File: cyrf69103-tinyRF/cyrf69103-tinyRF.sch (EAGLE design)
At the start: 32 parts

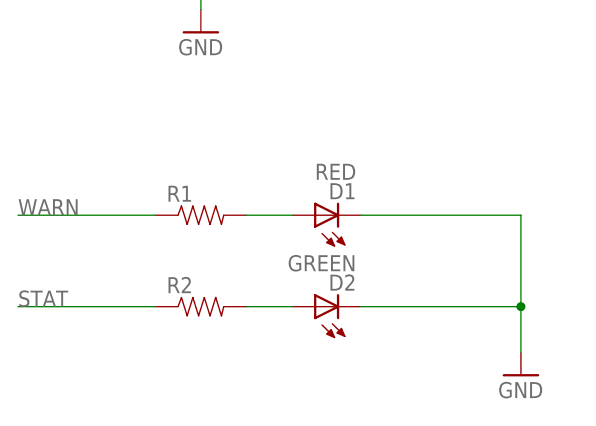
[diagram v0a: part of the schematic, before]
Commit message: Screwed up that last commit.  this update include changes to the production gerber folders.  Adds hackvana to the cyrf6936-BoB and cleans up the fab notes a bit.  Still need to standardize and parameterize the creation of the gerbers.
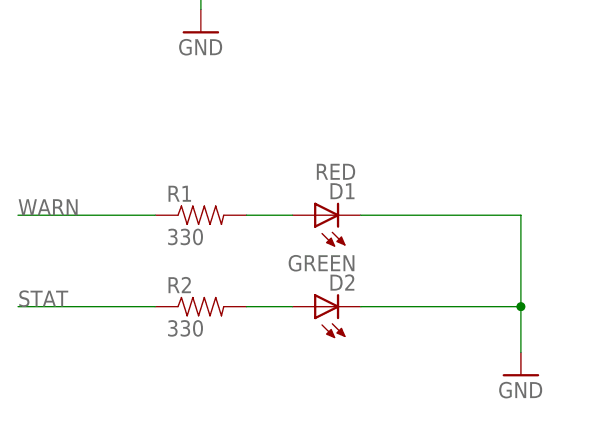
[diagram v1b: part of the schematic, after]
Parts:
- D1: PARTNO (none) -> LTST-C191TBKT
- D2: PARTNO (none) -> LTST-C190KGKT
- R1, R2: value (none) -> 330; PARTNO (none) -> CRCW0402330RJNED
- U$1: PARTNO (none) -> CYRF69103-40LFXC
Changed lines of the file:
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@@
 <grid distance="0.1" unitdist="inch" unit="inch" style="lines" multiple="1" display="no" altdistance="0.01" altunitdist="inch" altunit="inch"/>
 <layers>
-<layer number="1" name="Top" color="4" fill="1" visible="yes" active="no"/>
-<layer number="16" name="Bottom" color="1" fill="1" visible="yes" active="no"/>
-<layer number="17" name="Pads" color="2" fill="1" visible="yes" active="no"/>
-<layer number="18" name="Vias" color="2" fill="1" visible="yes" active="no"/>
-<layer number="19" name="Unrouted" color="6" fill="1" visible="yes" active="no"/>
-<layer number="20" name="Dimension" color="15" fill="1" visible="yes" active="no"/>
-<layer number="21" name="tPlace" color="16" fill="1" visible="yes" active="no"/>
-<layer number="22" name="bPlace" color="14" fill="1" visible="yes" active="no"/>
-<layer number="23" name="tOrigins" color="15" fill="1" visible="yes" active="no"/>
-<layer number="24" name="bOrigins" color="15" fill="1" visible="yes" active="no"/>
-<layer number="25" name="tNames" color="7" fill="1" visible="yes" active="no"/>
-<layer number="26" name="bNames" color="7" fill="1" visible="yes" active="no"/>
-<layer number="27" name="tValues" color="7" fill="1" visible="yes" active="no"/>
-<layer number="28" name="bValues" color="7" fill="1" visible="yes" active="no"/>
+<layer number="1" name="Top" color="4" fill="1" visible="no" active="no"/>
+<layer number="16" name="Bottom" color="1" fill="1" visible="no" active="no"/>
+<layer number="17" name="Pads" color="2" fill="1" visible="no" active="no"/>
+<layer number="18" name="Vias" color="2" fill="1" visible="no" active="no"/>
+<layer number="19" name="Unrouted" color="6" fill="1" visible="no" active="no"/>
+<layer number="20" name="Dimension" color="15" fill="1" visible="no" active="no"/>
+<layer number="21" name="tPlace" color="16" fill="1" visible="no" active="no"/>
+<layer number="22" name="bPlace" color="14" fill="1" visible="no" active="no"/>
+<layer number="23" name="tOrigins" color="15" fill="1" visible="no" active="no"/>
+<layer number="24" name="bOrigins" color="15" fill="1" visible="no" active="no"/>
+<layer number="25" name="tNames" color="7" fill="1" visible="no" active="no"/>
+<layer number="26" name="bNames" color="7" fill="1" visible="no" active="no"/>
+<layer number="27" name="tValues" color="7" fill="1" visible="no" active="no"/>
+<layer number="28" name="bValues" color="7" fill="1" visible="no" active="no"/>
 <layer number="29" name="tStop" color="7" fill="3" visible="no" active="no"/>
 <layer number="30" name="bStop" color="7" fill="6" visible="no" active="no"/>
@@
 <layer number="35" name="tGlue" color="7" fill="4" visible="no" active="no"/>
 <layer number="36" name="bGlue" color="7" fill="5" visible="no" active="no"/>
-<layer number="37" name="tTest" color="7" fill="1" visible="yes" active="no"/>
-<layer number="38" name="bTest" color="7" fill="1" visible="yes" active="no"/>
+<layer number="37" name="tTest" color="7" fill="1" visible="no" active="no"/>
+<layer number="38" name="bTest" color="7" fill="1" visible="no" active="no"/>
 <layer number="39" name="tKeepout" color="4" fill="11" visible="no" active="no"/>
 <layer number="40" name="bKeepout" color="1" fill="11" visible="no" active="no"/>
@@
 <layer number="44" name="Drills" color="7" fill="1" visible="no" active="no"/>
 <layer number="45" name="Holes" color="7" fill="1" visible="no" active="no"/>
-<layer number="46" name="Milling" color="3" fill="1" visible="yes" active="no"/>
-<layer number="47" name="Measures" color="7" fill="1" visible="yes" active="no"/>
-<layer number="48" name="Document" color="7" fill="1" visible="yes" active="no"/>
-<layer number="49" name="Reference" color="7" fill="1" visible="yes" active="no"/>
-<layer number="50" name="dxf" color="7" fill="1" visible="yes" active="no"/>
-<layer number="51" name="tDocu" color="6" fill="1" visible="yes" active="no"/>
-<layer number="52" name="bDocu" color="7" fill="1" visible="yes" active="no"/>
-<layer number="53" name="tPadExt" color="7" fill="1" visible="yes" active="no"/>
-<layer number="54" name="bPadExt" color="1" fill="1" visible="yes" active="no"/>
-<layer number="56" name="wert" color="7" fill="1" visible="yes" active="no"/>
+<layer number="46" name="Milling" color="3" fill="1" visible="no" active="no"/>
+<layer number="47" name="Measures" color="7" fill="1" visible="no" active="no"/>
+<layer number="48" name="Document" color="7" fill="1" visible="no" active="no"/>
+<layer number="49" name="Reference" color="7" fill="1" visible="no" active="no"/>
+<layer number="50" name="dxf" color="7" fill="1" visible="no" active="no"/>
+<layer number="51" name="tDocu" color="6" fill="1" visible="no" active="no"/>
+<layer number="52" name="bDocu" color="7" fill="1" visible="no" active="no"/>
+<layer number="53" name="tPadExt" color="7" fill="1" visible="no" active="no"/>
+<layer number="54" name="bPadExt" color="1" fill="1" visible="no" active="no"/>
+<layer number="56" name="wert" color="7" fill="1" visible="no" active="no"/>
 <layer number="91" name="Nets" color="2" fill="1" visible="yes" active="yes"/>
 <layer number="92" name="Busses" color="1" fill="1" visible="yes" active="yes"/>
@@
 </variantdefs>
 <classes>
-<class number="0" name="default" width="0" drill="0">
+<class number="0" name="default" width="0.1524" drill="0.3048">
+<clearance class="0" value="0.254"/>
 </class>
 </classes>
@@
 <part name="IRQ" library="JCM" deviceset="SOLDER_PAD" device=".05X.05" value="SOLDER_PAD.05X.05"/>
 <part name="GND" library="JCM" deviceset="SOLDER_PAD" device=".05X.05" value="SOLDER_PAD.05X.05"/>
-<part name="U$1" library="JCM" deviceset="CYRF69103" device=""/>
+<part name="U$1" library="JCM" deviceset="CYRF69103" device="">
+<attribute name="PARTNO" value="CYRF69103-40LFXC"/>
+</part>
 <part name="C2" library="SparkFun-Passives" deviceset="CAP" device="0402-CAP" value="0.47uF">
 <attribute name="PARTNO" value="GRM155R60J474KE19D"/>
@@
 <part name="SDATA" library="JCM" deviceset="SOLDER_PAD" device=".05X.05" value="SOLDER_PAD.05X.05"/>
 <part name="VCC_JMP" library="JCM" deviceset="SOLDER_PAD" device=".05X.05" value="SOLDER_PAD.05X.05"/>
-<part name="D2" library="SparkFun-LED" deviceset="LED-GREEN" device="0603" value="GREEN"/>
-<part name="D1" library="SparkFun-LED" deviceset="LED-RED" device="0603" value="RED"/>
+<part name="D2" library="SparkFun-LED" deviceset="LED-GREEN" device="0603" value="GREEN">
+<attribute name="PARTNO" value="LTST-C190KGKT"/>
+</part>
+<part name="D1" library="SparkFun-LED" deviceset="LED-RED" device="0603" value="RED">
+<attribute name="PARTNO" value="LTST-C191TBKT"/>
+</part>
 <part name="GND12" library="SparkFun-Aesthetics" deviceset="GND" device=""/>
-<part name="R1" library="SparkFun-Passives" deviceset="RESISTOR" device="0402-RES"/>
-<part name="R2" library="SparkFun-Passives" deviceset="RESISTOR" device="0402-RES"/>
+<part name="R1" library="SparkFun-Passives" deviceset="RESISTOR" device="0402-RES" value="330">
+<attribute name="PARTNO" value="CRCW0402330RJNED"/>
+</part>
+<part name="R2" library="SparkFun-Passives" deviceset="RESISTOR" device="0402-RES" value="330">
+<attribute name="PARTNO" value="CRCW0402330RJNED"/>
+</part>
 </parts>
 <sheets>
@@
 <attribute name="NAME" x="27.686" y="91.186" size="1.778" layer="95" rot="R180"/>
 </instance>
-<instance part="U$1" gate="G$1" x="104.14" y="83.82"/>
+<instance part="U$1" gate="G$1" x="104.14" y="83.82">
+<attribute name="PARTNO" x="104.14" y="83.82" size="1.778" layer="96" display="off"/>
+</instance>
 <instance part="C2" gate="G$1" x="134.62" y="132.08" rot="R90">
 <attribute name="PARTNO" x="134.62" y="132.08" size="1.778" layer="96" rot="R90" display="off"/>
@@
 <attribute name="NAME" x="147.574" y="172.974" size="1.778" layer="95"/>
 </instance>
-<instance part="D2" gate="G$1" x="50.8" y="33.02" rot="R90"/>
-<instance part="D1" gate="G$1" x="50.8" y="43.18" rot="R90"/>
+<instance part="D2" gate="G$1" x="50.8" y="33.02" rot="R90">
+<attribute name="PARTNO" x="50.8" y="33.02" size="1.778" layer="96" display="off"/>
+</instance>
+<instance part="D1" gate="G$1" x="50.8" y="43.18" rot="R90">
+<attribute name="PARTNO" x="50.8" y="43.18" size="1.778" layer="96" display="off"/>
+</instance>
 <instance part="GND12" gate="1" x="73.66" y="25.4"/>
-<instance part="R1" gate="G$1" x="38.1" y="43.18"/>
-<instance part="R2" gate="G$1" x="38.1" y="33.02"/>
+<instance part="R1" gate="G$1" x="38.1" y="43.18">
+<attribute name="PARTNO" x="38.1" y="43.18" size="1.778" layer="96" display="off"/>
+</instance>
+<instance part="R2" gate="G$1" x="38.1" y="33.02">
+<attribute name="PARTNO" x="38.1" y="33.02" size="1.778" layer="96" display="off"/>
+</instance>
 </instances>
 <busses>
